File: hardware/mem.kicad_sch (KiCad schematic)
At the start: 20 parts, among them U12 74HC373, U13 74HCT541, U7 28C256, U8 AS6C1008-xxP

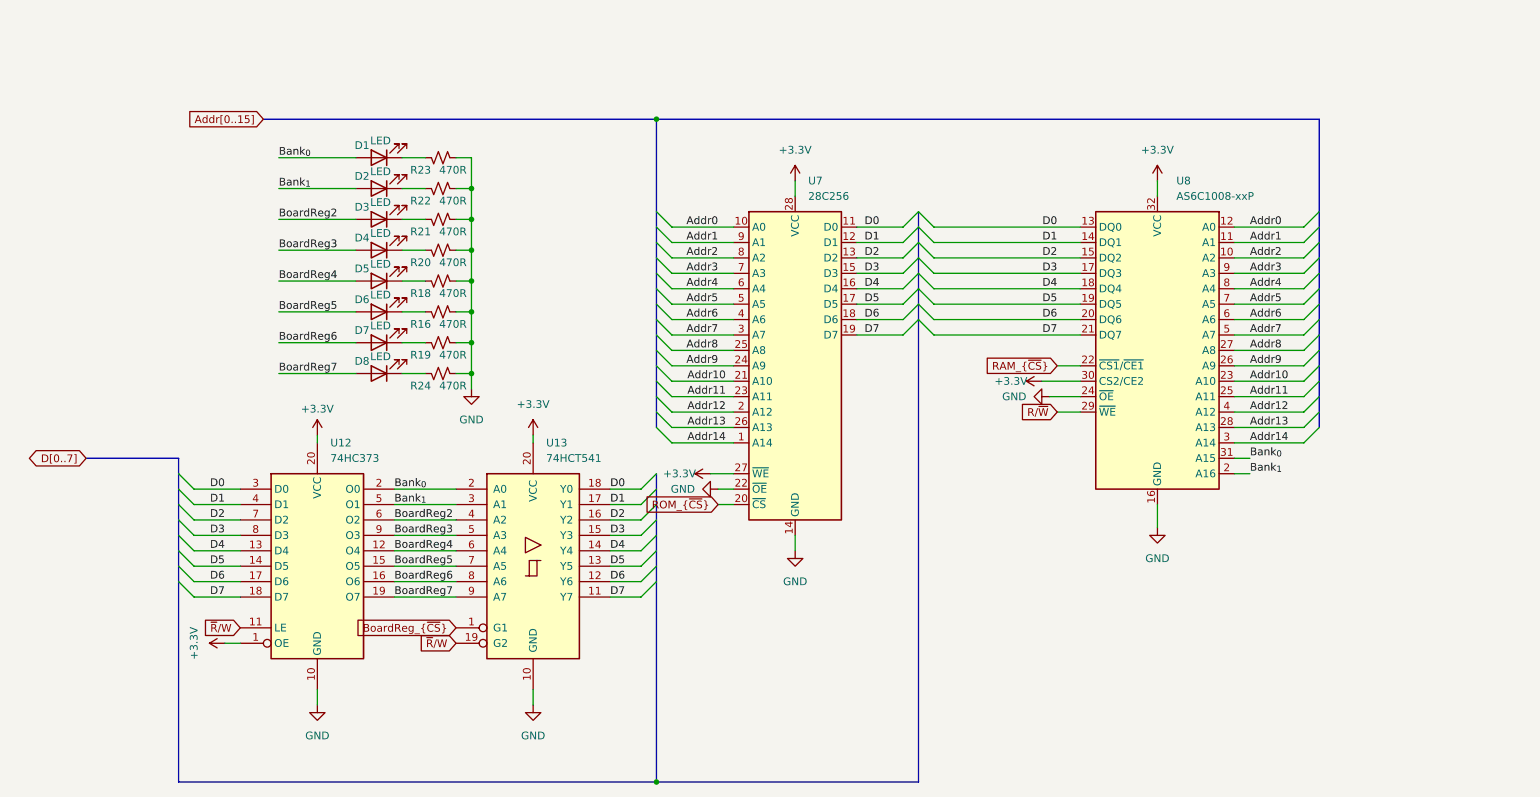
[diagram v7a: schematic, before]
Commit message: Fixed critical bugs on the system related to memory maping and IC selections
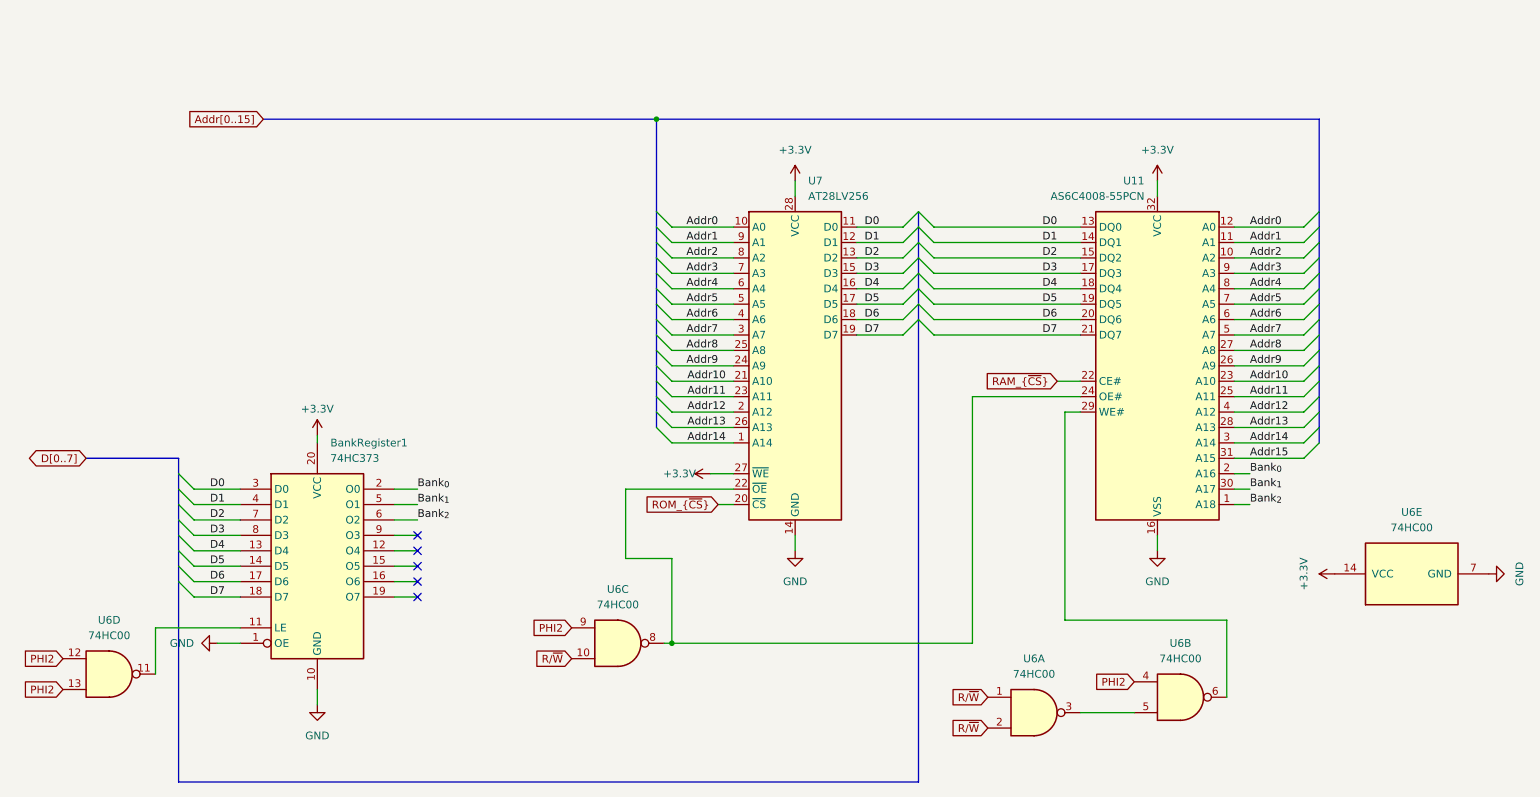
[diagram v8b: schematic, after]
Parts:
- removed D1, D2, D3, D4, D5, D6, D7, D8: LED, LED_SMD:LED_0805_2012Metric, symbol Device:LED
- removed R16, R18, R19, R20, R21, R22, R23, R24: 470R, Resistor_SMD:R_0603_1608Metric, symbol Device:R_Small_US
- removed U13: 74HCT541, symbol 74xx:74HCT541
- removed U8: AS6C1008-xxP, Package_DIP:DIP-32_W15.24mm, symbol Memory_RAM:AS6C1008-xxP
- added U11: AS6C4008-55PCN, Package_DIP:DIP-32_W15.24mm, symbol Memory_RAM:AS6C4008-55PCN
- added U6: 74HC00, Package_DIP:DIP-14_W7.62mm, symbol 74xx:74HC00
- U7: value 28C256 -> AT28LV256
- renumbered U12 to BankRegister1
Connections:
- net +3.3V: now also U11.32 (VCC), U6.14 (VCC); no longer BankRegister1.1 (OE)
- net Addr0: now also U11.12 (A0)
- net Addr1: now also U11.11 (A1)
- net Addr10: now also U11.23 (A10)
- net Addr11: now also U11.25 (A11)
- net Addr12: now also U11.4 (A12)
- net Addr13: now also U11.28 (A13)
- net Addr14: now also U11.3 (A14)
- net Addr2: now also U11.10 (A2)
- net Addr3: now also U11.9 (A3)
- net Addr4: now also U11.8 (A4)
- net Addr5: now also U11.7 (A5)
- net Addr6: now also U11.6 (A6)
- net Addr7: now also U11.5 (A7)
- net Addr8: now also U11.27 (A8)
- net Addr9: now also U11.26 (A9)
- net Bank_{0}: now also U11.2 (A16)
- net Bank_{1}: now also U11.30 (A17)
- net D0: now also U11.13 (DQ0)
- net D1: now also U11.14 (DQ1)
- net D2: now also U11.15 (DQ2)
- net D3: now also U11.17 (DQ3)
- net D4: now also U11.18 (DQ4)
- net D5: now also U11.19 (DQ5)
- net D6: now also U11.20 (DQ6)
- net D7: now also U11.21 (DQ7)
- net GND: now also BankRegister1.1 (OE), U11.16 (VSS), U6.7 (GND); no longer U7.22 (~{OE})
- net RAM_{~{CS}}: now also U11.22 (CE#)
- net R/~{W}: now also U6.1, U6.10, U6.2
- net BoardReg2 renamed Bank_{2}
- net Bank_{2}: now also U11.1 (A18)
- net BoardReg3: no longer names the net of BankRegister1.9 (O3)
- net BoardReg4: no longer names the net of BankRegister1.12 (O4)
- net BoardReg5: no longer names the net of BankRegister1.15 (O5)
- net BoardReg6: no longer names the net of BankRegister1.16 (O6)
- net BoardReg7: no longer names the net of BankRegister1.19 (O7)
- net ~{R}/W: no longer names the net of BankRegister1.11 (LE)
- net ~{R}/W: now also U6.11
- new net: U11.24 (OE#), U6.8, U7.22 (~{OE})
- new net: U11.29 (WE#), U6.6
- new net: U6.3, U6.5
- new net Addr15: U11.31 (A15)
- new net PHI2: U6.12, U6.13, U6.4, U6.9
- no-connect marks 0 -> 5
